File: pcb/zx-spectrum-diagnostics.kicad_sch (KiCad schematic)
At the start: 18 parts, among them J101 Conn_01x04, J102 Conn_01x03_Male, J103 Conn_01x03_Male, Q101 PMBT2222A, SW101 SW_SPST, U101 Pico, U102 Pico

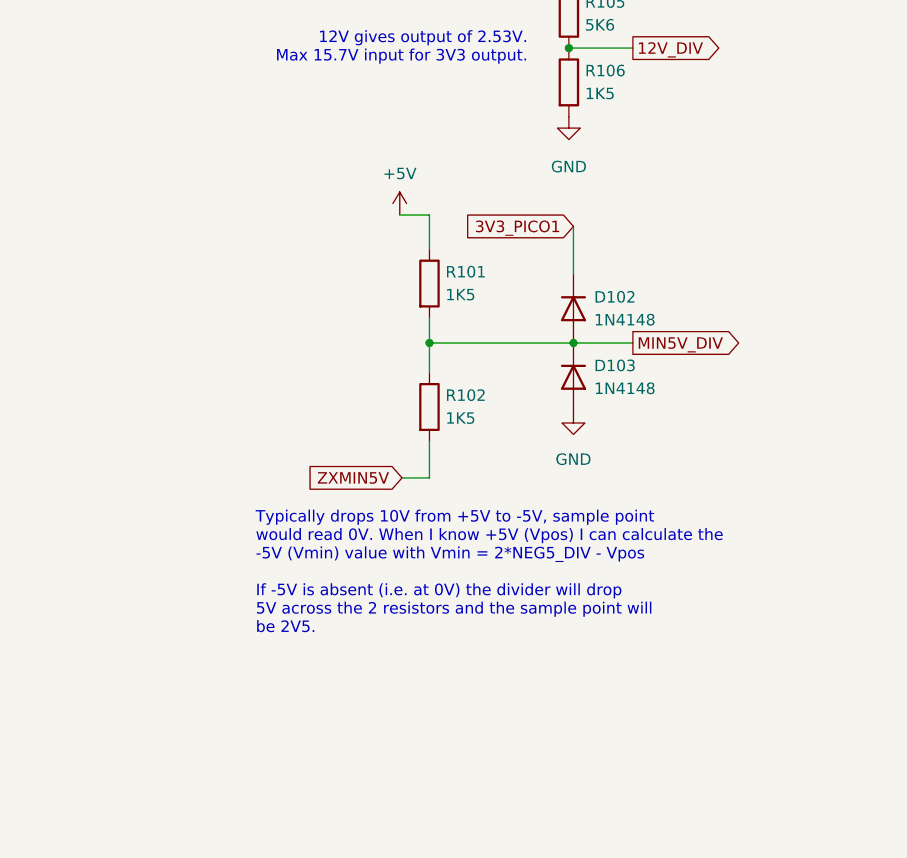
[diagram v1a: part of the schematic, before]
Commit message: update schematic and PCB with revised -5V voltage divider
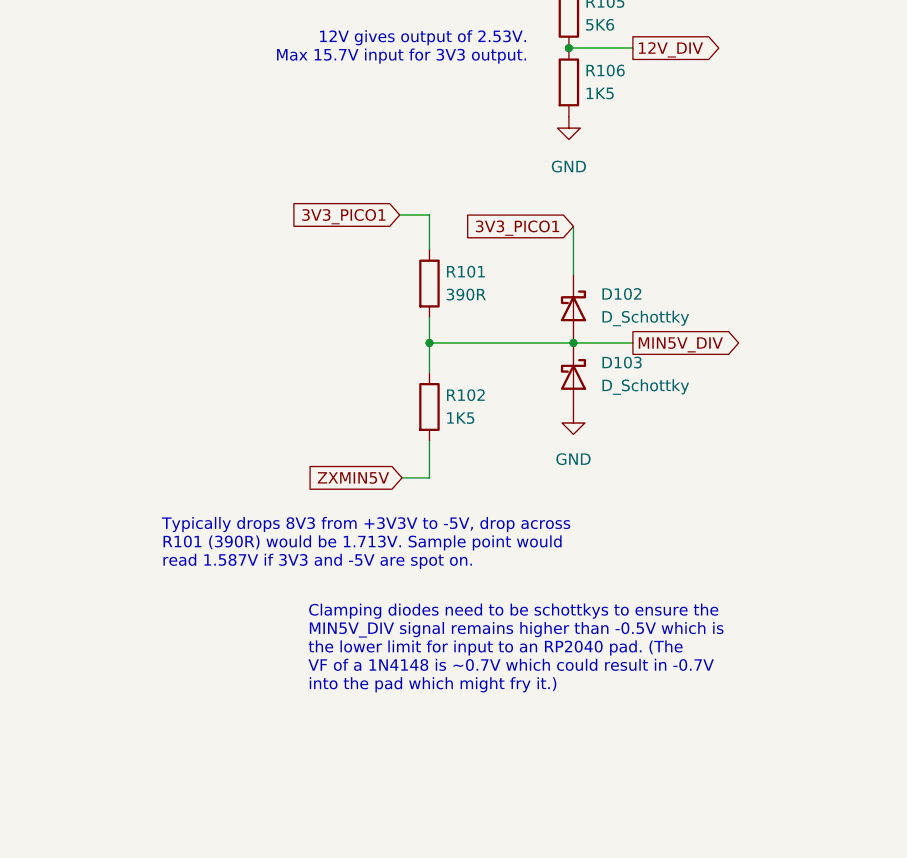
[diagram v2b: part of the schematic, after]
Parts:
- D102, D103: value 1N4148 -> D_Schottky; footprint Diode_SMD:D_SOD-123 -> Diode_SMD:D_1206_3216Metric_Pad1.42x1.75mm_HandSolder; symbol Diode:1N4148 -> Device:D_Schottky
- R101: value 1K5 -> 390R
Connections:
- net +5V: no longer R101.1
- net 3V3_PICO1: now also R101.1
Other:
- note added: "Clamping diodes need to be schottkys to ensure the MIN5V_DIV signal remains higher than -0.5V which is the lower limit for input to an RP2040 pad. (The VF of a 1N4148 is ~0.7V which could result in -0.7V into the pad which might fry it.)"
- note added: "Typically drops 8V3 from +3V3V to -5V, drop across R101 (390R) would be 1.713V. Sample point would read 1.587V if 3V3 and -5V are spot on."
- note removed: "Typically drops 10V from +5V to -5V, sample point would read 0V. When I know +5V (Vpos) I can calculate the -5V (Vmin) value with Vmin = 2*NEG5_DIV - Vpos If -5V is absent (i.e. at 0V) the divider will drop 5V across the 2 resistors and the sample point will be 2V5."
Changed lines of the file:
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@@
     (effects (font (size 1.27 1.27)) (justify right bottom))
   )
-  (text "Typically drops 10V from +5V to -5V, sample point\nwould read 0V. When I know +5V (Vpos) I can calculate the\n-5V (Vmin) value with Vmin = 2*NEG5_DIV - Vpos\n\nIf -5V is absent (i.e. at 0V) the divider will drop\n5V across the 2 resistors and the sample point will\nbe 2V5."
-    (at 224.536 121.158 0)
+  (text "Typically drops 8V3 from +3V3V to -5V, drop across\nR101 (390R) would be 1.713V. Sample point would\nread 1.587V if 3V3 and -5V are spot on."
+    (at 214.122 113.792 0)
+    (effects (font (size 1.27 1.27)) (justify left bottom))
+  )
+  (text "Clamping diodes need to be schottkys to ensure the\nMIN5V_DIV signal remains higher than -0.5V which is\nthe lower limit for input to an RP2040 pad. (The\nVF of a 1N4148 is ~0.7V which could result in -0.7V\ninto the pad which might fry it.)"
+    (at 230.378 127.508 0)
     (effects (font (size 1.27 1.27)) (justify left bottom))
   )
@@
     (property "Intersheet References" "${INTERSHEET_REFS}" (id 0) (at 61.7402 40.0526 0)
       (effects (font (size 1.27 1.27)) (justify left) hide)
+    )
+  )
+  (global_label "3V3_PICO1" (shape input) (at 240.538 74.422 180) (fields_autoplaced)
+    (effects (font (size 1.27 1.27)) (justify right))
+    (property "Intersheet References" "${INTERSHEET_REFS}" (id 0) (at 227.9649 74.5014 0)
+      (effects (font (size 1.27 1.27)) (justify right) hide)
     )
   )
@@
     (pin "1")
   )
-  (symbol (lib_id "power:+5V") (at 240.538 74.422 0) (unit 1)
-    (in_bom yes) (on_board yes) (fields_autoplaced)
-    (property "Reference" "#PWR0105" (id 0) (at 240.538 78.232 0)
-      (effects (font (size 1.27 1.27)) hide)
-    )
-    (property "Value" "+5V" (id 1) (at 240.538 69.85 0))
-    (property "Footprint" "" (id 2) (at 240.538 74.422 0)
-      (effects (font (size 1.27 1.27)) hide)
-    )
-    (property "Datasheet" "" (id 3) (at 240.538 74.422 0)
-      (effects (font (size 1.27 1.27)) hide)
-    )
-    (pin "1")
-  )
   (symbol (lib_id "power:GND") (at 18.796 134.874 0) (unit 1)
     (in_bom yes) (on_board yes) (fields_autoplaced)
@@
     (pin "2")
   )
-  (symbol (lib_id "Diode:1N4148") (at 259.842 92.456 270) (unit 1)
-    (in_bom yes) (on_board yes) (fields_autoplaced)
-    (property "Reference" "D103" (id 0) (at 262.128 91.1859 90)
+  (symbol (lib_id "Device:D_Schottky") (at 259.842 92.456 270) (unit 1)
+    (in_bom yes) (on_board yes) (fields_autoplaced)
+    (property "Reference" "D103" (id 0) (at 262.89 90.8684 90)
       (effects (font (size 1.27 1.27)) (justify left))
     )
-    (property "Value" "1N4148" (id 1) (at 262.128 93.7259 90)
+    (property "Value" "D_Schottky" (id 1) (at 262.89 93.4084 90)
       (effects (font (size 1.27 1.27)) (justify left))
     )
-    (property "Footprint" "Diode_SMD:D_SOD-123" (id 2) (at 259.842 92.456 0)
-      (effects (font (size 1.27 1.27)) hide)
-    )
-    (property "Datasheet" "https://assets.nexperia.com/documents/data-sheet/1N4148_1N4448.pdf" (id 3) (at 259.842 92.456 0)
+    (property "Footprint" "Diode_SMD:D_1206_3216Metric_Pad1.42x1.75mm_HandSolder" (id 2) (at 259.842 92.456 0)
+      (effects (font (size 1.27 1.27)) hide)
+    )
+    (property "Datasheet" "~" (id 3) (at 259.842 92.456 0)
       (effects (font (size 1.27 1.27)) hide)
     )
@@
     (pin "2")
   )
-  (symbol (lib_id "Diode:1N4148") (at 259.842 84.836 270) (unit 1)
-    (in_bom yes) (on_board yes) (fields_autoplaced)
-    (property "Reference" "D102" (id 0) (at 262.128 83.5659 90)
+  (symbol (lib_id "Device:D_Schottky") (at 259.842 84.836 270) (unit 1)
+    (in_bom yes) (on_board yes) (fields_autoplaced)
+    (property "Reference" "D102" (id 0) (at 262.89 83.2484 90)
       (effects (font (size 1.27 1.27)) (justify left))
     )
-    (property "Value" "1N4148" (id 1) (at 262.128 86.1059 90)
+    (property "Value" "D_Schottky" (id 1) (at 262.89 85.7884 90)
       (effects (font (size 1.27 1.27)) (justify left))
     )
-    (property "Footprint" "Diode_SMD:D_SOD-123" (id 2) (at 259.842 84.836 0)
-      (effects (font (size 1.27 1.27)) hide)
-    )
-    (property "Datasheet" "https://assets.nexperia.com/documents/data-sheet/1N4148_1N4448.pdf" (id 3) (at 259.842 84.836 0)
+    (property "Footprint" "Diode_SMD:D_1206_3216Metric_Pad1.42x1.75mm_HandSolder" (id 2) (at 259.842 84.836 0)
+      (effects (font (size 1.27 1.27)) hide)
+    )
+    (property "Datasheet" "~" (id 3) (at 259.842 84.836 0)
       (effects (font (size 1.27 1.27)) hide)
     )
@@
       (effects (font (size 1.27 1.27)) (justify left))
     )
-    (property "Value" "1K5" (id 1) (at 245.618 83.3119 0)
+    (property "Value" "390R" (id 1) (at 245.618 83.3119 0)
       (effects (font (size 1.27 1.27)) (justify left))
     )
@@
       (reference "#PWR0104") (unit 1) (value "+5V") (footprint "")
     )
-    (path "/96493c2b-7188-4bc8-b7e0-65f41e6501e3"
-      (reference "#PWR0105") (unit 1) (value "+5V") (footprint "")
-    )
     (path "/7b48b197-226e-41e4-b518-808ba2aee750"
       (reference "#PWR0106") (unit 1) (value "+5V") (footprint "")
@@
     )
     (path "/d9d4c412-10f6-47b7-9c11-43e0dd422b75"
-      (reference "D102") (unit 1) (value "1N4148") (footprint "Diode_SMD:D_SOD-123")
+      (reference "D102") (unit 1) (value "D_Schottky") (footprint "Diode_SMD:D_1206_3216Metric_Pad1.42x1.75mm_HandSolder")
     )
     (path "/d3364c3f-7456-4539-86a5-d88591e950f5"
-      (reference "D103") (unit 1) (value "1N4148") (footprint "Diode_SMD:D_SOD-123")
+      (reference "D103") (unit 1) (value "D_Schottky") (footprint "Diode_SMD:D_1206_3216Metric_Pad1.42x1.75mm_HandSolder")
     )
     (path "/4306a88c-b446-420a-8a4d-c6b820db0ec2"
@@
     )
     (path "/f338c199-5c84-47b5-961e-f046c86e3290"
-      (reference "R101") (unit 1) (value "1K5") (footprint "Resistor_SMD:R_1206_3216Metric_Pad1.30x1.75mm_HandSolder")
+      (reference "R101") (unit 1) (value "390R") (footprint "Resistor_SMD:R_1206_3216Metric_Pad1.30x1.75mm_HandSolder")
     )
     (path "/e1ce659c-6ff5-46ac-8196-738a93ea61ec"
